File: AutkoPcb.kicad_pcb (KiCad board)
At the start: 2 copper layers, 200 x 120 mm, 45 parts, among them IC201 TEENSY_4.1, J101 Conn_01x06_Male, J102 Conn_01x04_Male, J103 Conn_01x05_Male, J104 Conn_01x04_Male, J105 Conn_01x02_Male, J106 Conn_01x02_Male, J107 Conn_01x02_Male, J108 Conn_01x05_Male, J401 Conn_01x03_Male, J501 Conn_01x03_Male, J601 Conn_01x04_Male, J701 Conn_01x04_Male, J801 Conn_01x04_Male, J901 Screw_Terminal_01x02, SW1001 SW_Push, SW1101 SW_Push, SW1201 SW_Push, SW1301 SW_Push, U901 AZ1117-3.3

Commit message: initial PCB layout is done
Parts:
- moved C702 65.8 mm to (127.4, 121.1), turned to 90 degrees
- moved C802 60.9 mm to (126.6, 104.6), turned to 90 degrees
- moved C602 59.2 mm to (128.1, 112.8), turned to 90 degrees
- moved C701 59.0 mm to (123.4, 121.1), turned to 90 degrees
- moved C801 53.1 mm to (122.1, 104.6), turned to 90 degrees
- moved J901 51.2 mm to (109.5, 45.6), turned to -90 degrees
- moved C601 50.9 mm to (123.6, 112.9), turned to 90 degrees
- moved R1001 47.6 mm to (125.7, 127.8), turned to 180 degrees
- moved J105 46.8 mm to (115.9, 83.9)
- moved C401 46.8 mm to (108.5, 66.3)
- moved C402 46.6 mm to (104.0, 66.4)
- moved J401 46.0 mm to (113.0, 66.3)
- moved J501 46.0 mm to (113.0, 73.8)
- moved C502 45.8 mm to (104.2, 73.9)
- moved C501 45.6 mm to (108.5, 73.8)
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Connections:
- net Net-(D901-Pad1) renamed /Power/VIN_CONN
- net Net-(D901-Pad2) renamed /Power/VIN_FUSE
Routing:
- net +3.3V: track 0.00 -> 239.2 mm
- net VCC: track 0.00 -> 74.0 mm
- net +5V: track 0.00 -> 62.9 mm
- net /ULTRAD3_B: track 0.00 -> 61.7 mm, vias 0 -> 2
- net /ULTRAD3_A: track 0.00 -> 60.7 mm, vias 0 -> 2
- net /ULTRAD1_B: track 0.00 -> 43.7 mm
- net /DISP_SCK: track 0.00 -> 43.5 mm
- net /ULTRAD1_A: track 0.00 -> 40.2 mm
- net /STEERING: track 0.00 -> 37.1 mm
- net /DISP_MISO: track 0.00 -> 33.2 mm
- net /TOF_INT: track 0.00 -> 31.3 mm, vias 0 -> 2
- net /DISP_MOSI: track 0.00 -> 29.7 mm
- net /BUTTON_D: track 0.00 -> 27.8 mm, vias 0 -> 1
- net /CAMERA_SERVO_A: track 0.00 -> 27.7 mm
- net /ULTRAD2_B: track 0.00 -> 26.9 mm
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- added copper zone on B.Cu, net GND
- added copper zone on F.Cu, net GND
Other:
- board size 200 x 120 mm -> 83.8 x 120 mm

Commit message: [FEAT] schematic and alyout finished but need to be revieved
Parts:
- added J104: Conn_01x04_Male, Connector_PinHeader_2.54mm:PinHeader_1x04_P2.54mm_Vertical, F.Cu at (101.4, 87.0)
- added J105: Conn_01x04_Male, Connector_PinHeader_2.54mm:PinHeader_1x04_P2.54mm_Vertical, F.Cu at (101.2, 106.6)
- added J106: Conn_01x11_Male, Connector_PinSocket_2.54mm:PinSocket_1x11_P2.54mm_Vertical, F.Cu at (179.8, 117.5)
- added J902: Barrel_Jack_MountingPin, Connector_BarrelJack:BarrelJack_Wuerth_6941xx301002, F.Cu at (113.5, 42.4)
- J901: value Screw_Terminal_01x02 -> Barrel_Jack_MountingPin; footprint TerminalBlock:TerminalBlock_Altech_AK300-2_P5.00mm -> Connector_BarrelJack:BarrelJack_Wuerth_6941xx301002
- moved C902 49.3 mm to (124.5, 52.8)
- moved C901 49.2 mm to (124.5, 48.8)
- moved C904 46.5 mm to (130.5, 48.5)
- moved C903 44.0 mm to (130.5, 52.8)
- moved U901 36.5 mm to (131.3, 56.0), turned to 180 degrees
- moved J801 35.0 mm to (110.6, 136.8), turned to -90 degrees
- moved DC901 33.1 mm to (159.6, 47.0), turned to -90 degrees
- moved C801 29.5 mm to (112.4, 132.4), turned to 180 degrees
- moved C802 27.8 mm to (112.4, 128.4), turned to 180 degrees
- moved J601 25.9 mm to (118.7, 136.8), turned to -90 degrees
- moved SW1001 25.5 mm to (110.0, 105.1)
- moved C1001 25.5 mm to (118.5, 104.6)
- moved C1101 25.5 mm to (118.5, 109.9)
- moved C1201 25.5 mm to (118.5, 115.2)
- moved C1301 25.5 mm to (118.5, 120.8)
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- renumbered J103 to J107, J104 to J108, J105 to J109, J106 to J110, J107 to J111, J108 to J112
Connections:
- D901 pad 3: unconnected-(D901-Pad3) -> /Power/VIN_CONN2
- IC201 pad 1: unconnected-(IC201-Pad1) -> /TX1_NC
- IC201 pad 14: unconnected-(IC201-Pad14) -> /A0_NC
- IC201 pad 15: unconnected-(IC201-Pad15) -> /A1_NC
- IC201 pad 20: unconnected-(IC201-Pad20) -> /A6_NC
- IC201 pad 21: unconnected-(IC201-Pad21) -> /A7_NC
- IC201 pad 22: unconnected-(IC201-Pad22) -> /A8_NC
- IC201 pad 23: unconnected-(IC201-Pad23) -> /A9_NC
- IC201 pad 24: unconnected-(IC201-Pad24) -> /A10_NC
- IC201 pad 25: unconnected-(IC201-Pad25) -> /A11_NC
- IC201 pad 39: unconnected-(IC201-Pad39) -> /A15_NC
- IC201 pad 46: unconnected-(IC201-Pad46) -> /Tensee/PROGRAM_NC
- IC201 pad 47: unconnected-(IC201-Pad47) -> /Tensee/ON_OFF_NC
- IC201 pad 50: unconnected-(IC201-Pad50) -> /D+_NC
- IC201 pad 51: unconnected-(IC201-Pad51) -> /D-_NC
- IC201 pad 55: unconnected-(IC201-Pad55) -> /Tensee/VIN_NC
- IC201 pad 57: unconnected-(IC201-Pad57) -> /RX1_NC
- IC201 pad 68: unconnected-(IC201-Pad68) -> /V_USB_NC
- IC201 pad 7: unconnected-(IC201-Pad7) -> /RX2_NC
- IC201 pad 8: unconnected-(IC201-Pad8) -> /TX2_NC
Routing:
- net +3.3V: track 239.2 -> 343.9 mm
- net VCC: track 74.0 -> 127.3 mm
- net /TX2_NC: track 0.00 -> 51.1 mm
- net /RX2_NC: track 0.00 -> 49.6 mm
- net /A11_NC: track 0.00 -> 45.4 mm, vias 0 -> 2
- net /A10_NC: track 0.00 -> 44.7 mm
- net +5V: track 62.9 -> 104.1 mm
- net /A0_NC: track 0.00 -> 40.7 mm, vias 0 -> 4
- net /TX1_NC: track 0.00 -> 39.1 mm, vias 0 -> 2
- net /RX1_NC: track 0.00 -> 39.0 mm, vias 0 -> 2
- net /A1_NC: track 0.00 -> 38.7 mm, vias 0 -> 4
- net /A6_NC: track 0.00 -> 36.8 mm
- net /A7_NC: track 0.00 -> 36.3 mm
- net /A8_NC: track 0.00 -> 35.5 mm
- net /A9_NC: track 0.00 -> 34.3 mm
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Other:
- board size 83.8 x 120 mm -> 83.8 x 113.2 mm
- board text added: "3.3V"
- board text added: "A"
- board text added: "A0"
- board text added: "A1"
- board text added: "A10"
- board text added: "A11"
- board text added: "A15"
- board text added: "A5"
- board text added: "A7"
- board text added: "A8"
- board text added: "A9"
- board text added: "B"
- board text added: "BUTTONS"
- board text added: "CAM_A"
- board text added: "CS"
- board text added: "EN"
- board text added: "ENCODER"
- board text added: "ENCODER_A"
- board text added: "ENCODER_B"
- board text added: "GND"
- board text added: "GPS"
- board text added: "IMU"
- board text added: "IN"
- board text added: "INT"
- board text added: "MISO"
- board text added: "MOSI"
- board text added: "RX"
- board text added: "RX1"
- board text added: "RX2"
- board text added: "SCK"
- board text added: "SCL"
- board text added: "SDA"
- board text added: "SERVO_CAM_A"
- board text added: "SERVO_CAM_B"
- board text added: "SPEED"
- board text added: "STERING"
- board text added: "TOF"
- board text added: "TX"
- board text added: "TX1"
- board text added: "TX2"
- board text added: "ULTRAD1"
- board text added: "ULTRAD2"
- board text added: "ULTRAD3"
- board text added: "VCC"
- board text added: "VOLTMETER"

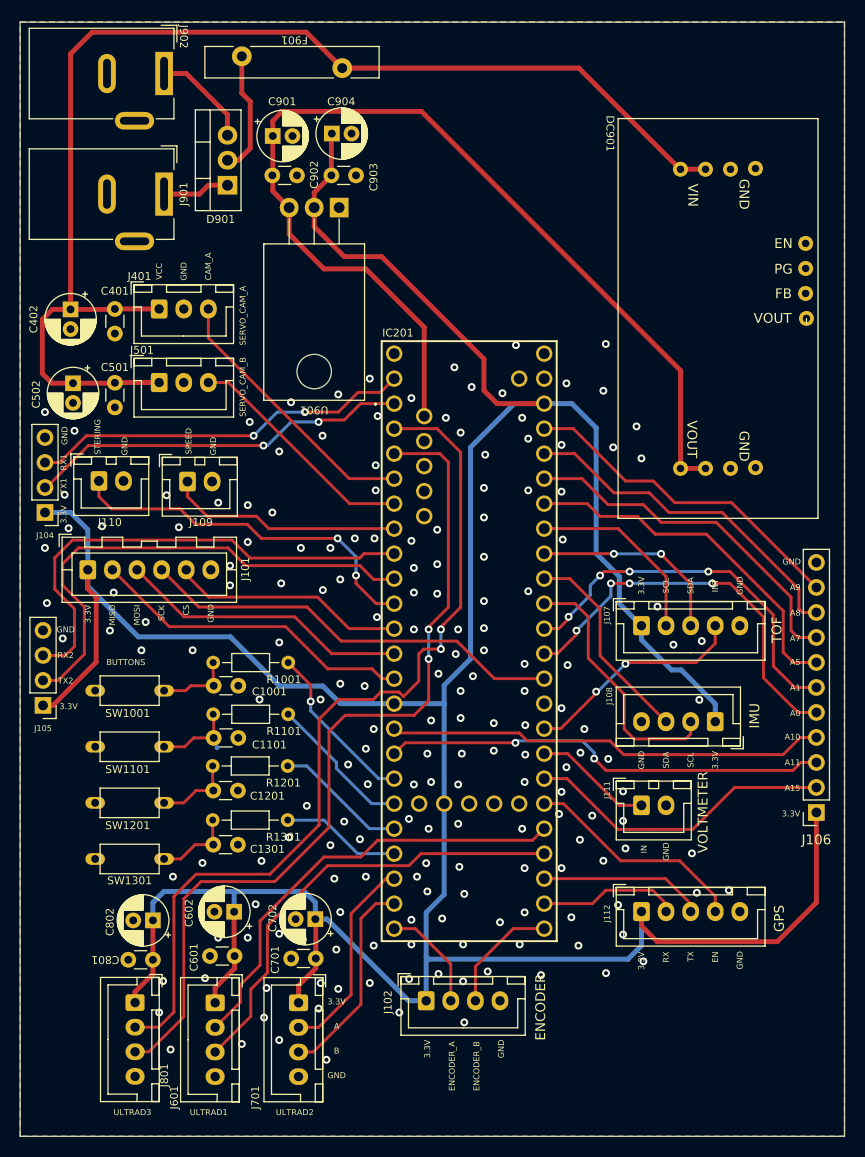
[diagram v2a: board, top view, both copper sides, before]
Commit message: [FIX] changed type of barrel jack to correct one
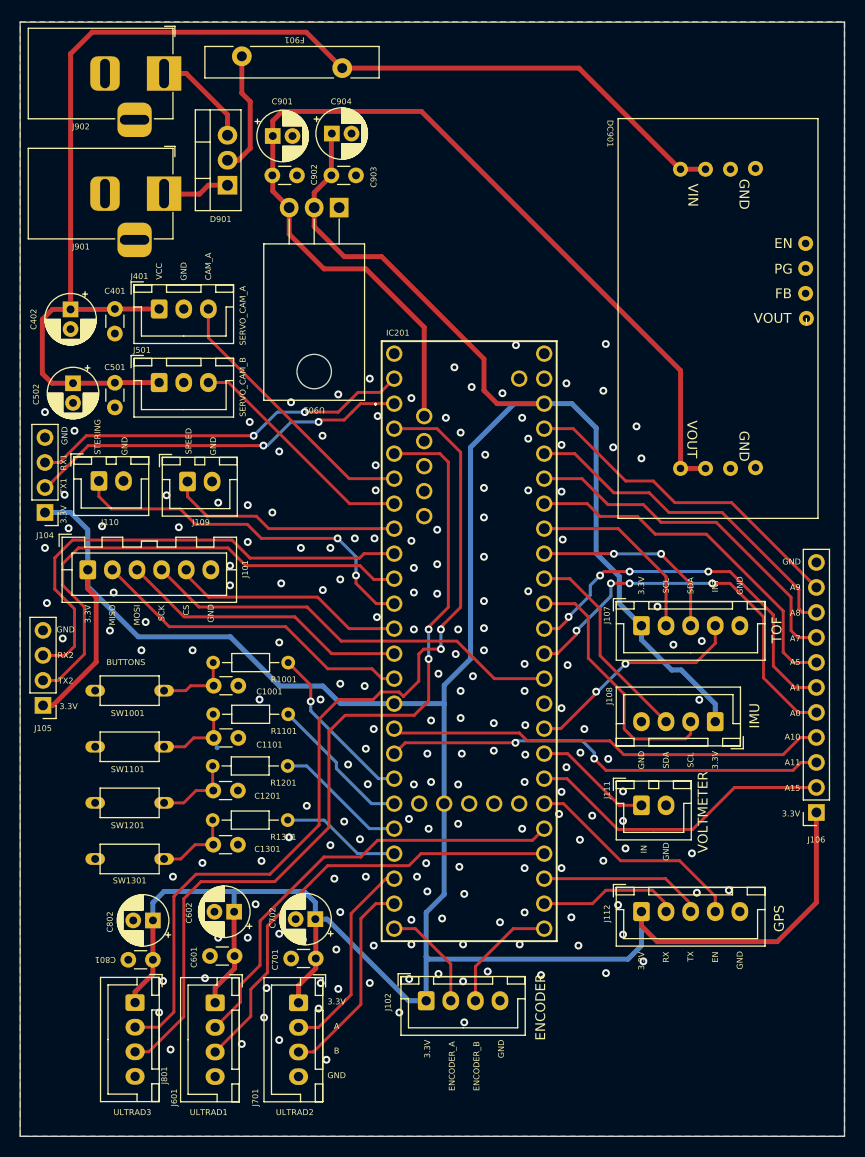
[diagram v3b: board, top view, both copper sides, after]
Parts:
- J901, J902: footprint Connector_BarrelJack:BarrelJack_Wuerth_6941xx301002 -> Connector_BarrelJack:BarrelJack_Horizontal
- turned J901 to 0 degrees
- turned J902 to 0 degrees

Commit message: schematic update after meeting
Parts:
- removed C904: 10uF, Capacitor_THT:CP_Radial_D5.0mm_P2.00mm
- added F902: Fuse, Fuse:Fuse_Bourns_MF-RHT1000, F.Cu at (196.2, 62.2)
- added J103: JST 2.56mm, Connector_PinHeader_2.54mm:PinHeader_1x04_P2.54mm_Vertical, F.Cu at (194.2, 89.9)
- added J113: JST 2.56mm, Connector_JST:JST_XH_B3B-XH-A_1x03_P2.50mm_Vertical, F.Cu at (199.9, 90.9)
- added J903: Barrel_Jack_MountingPin, Connector_BarrelJack:BarrelJack_Horizontal, F.Cu at (201.2, 74.3)
- added J904: ARK 5mm, TerminalBlock_Philmore:TerminalBlock_Philmore_TB132_1x02_P5.00mm_Horizontal, F.Cu at (212.4, 74.2)
- added J905: JST 2.54mm, Connector_JST:JST_XH_B2B-XH-A_1x02_P2.50mm_Vertical, F.Cu at (224.4, 79.5)
- added J906: JST 2.54mm, Connector_JST:JST_XH_B2B-XH-A_1x02_P2.50mm_Vertical, F.Cu at (224.4, 71.8)
- added J907: JST 2.56mm, Connector_JST:JST_XH_B4B-XH-A_1x04_P2.50mm_Vertical, F.Cu at (214.3, 64.0)
- added R101: 4.7k, Resistor_THT:R_Axial_DIN0204_L3.6mm_D1.6mm_P7.62mm_Horizontal, F.Cu at (208.5, 100.1)
- added R102: 4.7k, Resistor_THT:R_Axial_DIN0204_L3.6mm_D1.6mm_P7.62mm_Horizontal, F.Cu at (208.5, 96.9)
- added R103: 4.7k, Resistor_THT:R_Axial_DIN0204_L3.6mm_D1.6mm_P7.62mm_Horizontal, F.Cu at (197.9, 100.1)
- added R104: 4.7k, Resistor_THT:R_Axial_DIN0204_L3.6mm_D1.6mm_P7.62mm_Horizontal, F.Cu at (197.9, 96.9)
- C901: value 10uF -> 100nF; footprint Capacitor_THT:CP_Radial_D5.0mm_P2.00mm -> Capacitor_THT:C_Disc_D3.0mm_W1.6mm_P2.50mm
- C903: value 100nF -> 10uF; footprint Capacitor_THT:C_Disc_D3.0mm_W1.6mm_P2.50mm -> Capacitor_THT:CP_Radial_D5.0mm_P2.00mm
- J101: value Conn_01x06_Male -> JST 2.56mm
- J102, J104, J601, J701, J801: value Conn_01x04_Male -> JST 2.56mm
- J105: value Conn_01x04_Male -> JST 2.56mm; footprint Connector_PinHeader_2.54mm:PinHeader_1x04_P2.54mm_Vertical -> Connector_JST:JST_XH_B4B-XH-A_1x04_P2.50mm_Vertical
- J106: value Conn_01x11_Male -> Conn_01x10_Male; footprint Connector_PinSocket_2.54mm:PinSocket_1x11_P2.54mm_Vertical -> Connector_PinHeader_2.54mm:PinHeader_1x10_P2.54mm_Vertical
- J107: value Conn_01x05_Male -> JST 2.56mm; footprint Connector_JST:JST_XH_B5B-XH-A_1x05_P2.50mm_Vertical -> Connector_JST:JST_XH_B2B-XH-A_1x02_P2.50mm_Vertical
- J108: value Conn_01x04_Male -> JST 2.56mm; footprint Connector_JST:JST_XH_B4B-XH-A_1x04_P2.50mm_Vertical -> Connector_JST:JST_XH_B2B-XH-A_1x02_P2.50mm_Vertical
- J109, J111: value Conn_01x02_Male -> JST 2.56mm; footprint Connector_JST:JST_XH_B2B-XH-A_1x02_P2.50mm_Vertical -> Connector_JST:JST_XH_B5B-XH-A_1x05_P2.50mm_Vertical
- J110: value Conn_01x02_Male -> JST 2.56mm; footprint Connector_JST:JST_XH_B2B-XH-A_1x02_P2.50mm_Vertical -> Connector_JST:JST_XH_B4B-XH-A_1x04_P2.50mm_Vertical
- J112: value Conn_01x05_Male -> JST 2.56mm; footprint Connector_JST:JST_XH_B5B-XH-A_1x05_P2.50mm_Vertical -> Connector_JST:JST_XH_B3B-XH-A_1x03_P2.50mm_Vertical
- J901: value Barrel_Jack_MountingPin -> ARK 5mm; footprint Connector_BarrelJack:BarrelJack_Horizontal -> TerminalBlock_Philmore:TerminalBlock_Philmore_TB132_1x02_P5.00mm_Horizontal
- R1001, R1101, R1201, R1301: value R -> 100R
- moved J105 113.2 mm to (192.0, 39.0), turned to -90 degrees
- moved R1301 9.88 mm to (116.2, 118.8), turned to 0 degrees
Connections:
- C1001 pad 1: Net-(C1001-Pad1) -> /BUTTON_A
- C1101 pad 1: Net-(C1101-Pad1) -> /BUTTON_B
- C1201 pad 1: Net-(C1201-Pad1) -> /BUTTON_C
- C1301 pad 1: Net-(C1301-Pad1) -> /BUTTON_D
- C401 pad 1: VCC -> +5V
- C402 pad 1: VCC -> +5V
- C501 pad 1: VCC -> +5V
- C502 pad 1: VCC -> +5V
- C902 pad 1: +5V -> +3.3V
- D901 pad 1: /Power/VIN_CONN -> Net-(D901-Pad1)
- D901 pad 3: /Power/VIN_CONN2 -> Net-(D901-Pad3)
- F901 pad 1: /Power/VIN_FUSE -> /Power/VIN_CONN
- F901 pad 2: VCC -> Net-(D901-Pad1)
- IC201 pad 22: /A8_NC -> /STEERING1
- IC201 pad 23: /A9_NC -> /STEERING2
- IC201 pad 40: /VOLTMETER -> /A16_NC
- IC201 pad 42: +3.3V -> unconnected-(IC201-Pad42)
- IC201 pad 44: +3.3V -> unconnected-(IC201-Pad44)
- IC201 pad 52: +5V -> unconnected-(IC201-Pad52)
- IC201 pad 53: +3.3V -> unconnected-(IC201-Pad53)
- IC201 pad 55: /Tensee/VIN_NC -> +5V
- IC201 pad 6: /SPEED -> /SPEED1
- IC201 pad 9: /STEERING -> /SPEED2
- J104 pad 2: /TX1_NC -> /TX2_NC
- J104 pad 3: /RX1_NC -> /RX2_NC
- J105 pad 1: +3.3V -> /V_USB_NC
- J105 pad 2: /TX2_NC -> /D-_NC
- J105 pad 3: /RX2_NC -> /D+_NC
- J106 pad 10: /A9_NC -> GND
- J106 pad 2: /A15_NC -> /A16_NC
- J106 pad 3: /A11_NC -> /A15_NC
- J106 pad 4: /A10_NC -> /A11_NC
- J106 pad 5: /A0_NC -> /A10_NC
- J106 pad 6: /A1_NC -> /A0_NC
- J106 pad 7: /A6_NC -> /A1_NC
- J106 pad 8: /A7_NC -> /A6_NC
- J106 pad 9: /A8_NC -> /A7_NC
- J107 pad 1: +3.3V -> /SPEED1
- J107 pad 2: /TOF_SCL -> GND
- J108 pad 1: +3.3V -> /SPEED2
- J108 pad 2: /IMU_SCL -> GND
- J109 pad 1: /SPEED -> +3.3V
- J109 pad 2: GND -> /TOF_SCL
- J110 pad 1: /STEERING -> +3.3V
- J110 pad 2: GND -> /IMU_SCL
- J111 pad 1: /VOLTMETER -> +3.3V
- J111 pad 2: GND -> /GPS_RX
- J112 pad 1: +3.3V -> Net-(J112-Pad1)
- J112 pad 2: /GPS_RX -> /STEERING1
- J112 pad 3: /GPS_TX -> GND
- J401 pad 1: VCC -> +5V
- J501 pad 1: VCC -> +5V
- J901 pad 1: /Power/VIN_CONN -> GND
- J901 pad 2: GND -> /Power/VIN_CONN
- J902 pad 1: /Power/VIN_CONN2 -> /Power/VIN_CONN
- R1001 pad 2: Net-(C1001-Pad1) -> Net-(R1001-Pad2)
- R1101 pad 2: Net-(C1101-Pad1) -> Net-(R1101-Pad2)
- R1201 pad 2: Net-(C1201-Pad1) -> Net-(R1201-Pad2)
- R1301 pad 2: Net-(C1301-Pad1) -> Net-(R1301-Pad2)
- SW1001 pad 1: Net-(C1001-Pad1) -> Net-(R1001-Pad2)
- SW1101 pad 1: Net-(C1101-Pad1) -> Net-(R1101-Pad2)
- SW1201 pad 1: Net-(C1201-Pad1) -> Net-(R1201-Pad2)
- SW1301 pad 1: Net-(C1301-Pad1) -> Net-(R1301-Pad2)
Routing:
- net VCC: track 127.3 -> 0.00 mm
- net +5V: track 104.1 -> 231.4 mm
- net +3.3V: track 343.9 -> 446.1 mm, vias 0 -> 6
- net GND: track 0.00 -> 77.6 mm
- net /A11_NC: track 45.4 -> 0.00 mm, vias 2 -> 0
- net /A15_NC: track 31.6 -> 76.9 mm, vias 0 -> 2
- net /TX2_NC: track 51.1 -> 90.2 mm, vias 0 -> 2
- net /TX1_NC: track 39.1 -> 0.00 mm, vias 2 -> 0
- net /RX2_NC: track 49.6 -> 88.6 mm, vias 0 -> 2
- net /RX1_NC: track 39.0 -> 0.00 mm, vias 2 -> 0
- net /A1_NC: track 38.7 -> 0.00 mm, vias 4 -> 0
- net /STEERING: track 37.7 -> 0.00 mm, vias 2 -> 0
- net /A8_NC: track 35.5 -> 0.00 mm
- net /A7_NC: track 36.3 -> 71.8 mm
- net /A9_NC: track 34.3 -> 0.00 mm
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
